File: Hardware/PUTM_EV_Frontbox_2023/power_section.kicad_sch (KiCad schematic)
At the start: 41 parts, among them U19 TLV743P, U20 LM4040DBZ-5, U4 TLV743P, U5 TLV743P, U6 BD50FC0FP, U7 LM62440-Q1

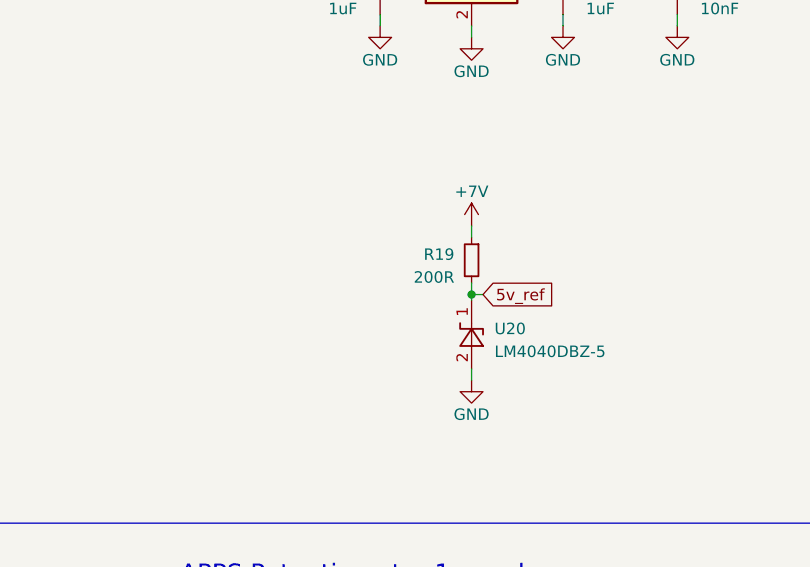
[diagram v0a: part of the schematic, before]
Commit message: Redid component placement
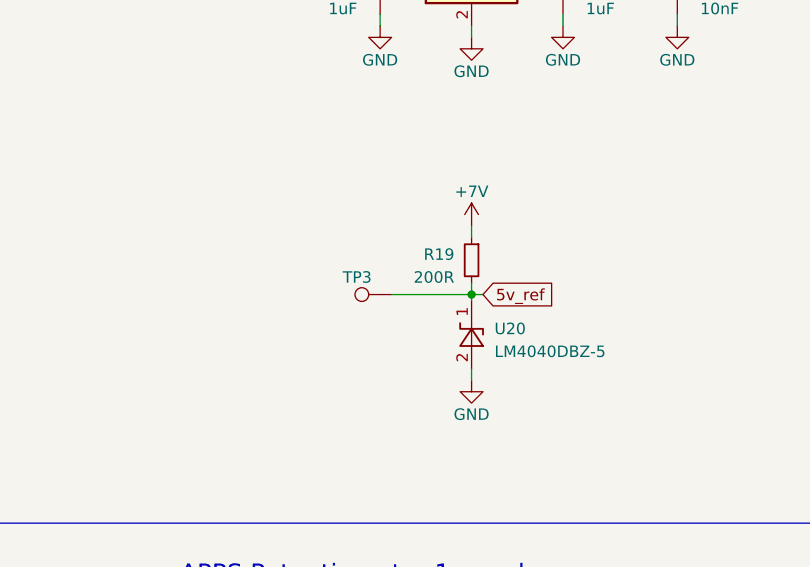
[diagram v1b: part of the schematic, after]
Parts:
- added TP3: TestPoint, TestPoint:TestPoint_Pad_1.0x1.0mm, symbol Connector:TestPoint
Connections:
- net 5v_ref: now also TP3.1
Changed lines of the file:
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@@
+    (stroke (width 0) (type default))
+  )
+  (wire (pts (xy 222.885 66.675) (xy 231.775 66.675))
     (stroke (width 0) (type default))
   )
@@
     )
   )
+  (symbol (lib_id "Connector:TestPoint") (at 222.885 66.675 90) (unit 1)
+    (in_bom yes) (on_board yes) (dnp no)
+    (property "Reference" "TP3" (at 219.075 64.77 90)
+      (effects (font (size 1.27 1.27)))
+    )
+    (property "Value" "TestPoint" (at 219.583 64.77 90)
+      (effects (font (size 1.27 1.27)) hide)
+    )
+    (property "Footprint" "TestPoint:TestPoint_Pad_1.0x1.0mm" (at 222.885 61.595 0)
+      (effects (font (size 1.27 1.27)) hide)
+    )
+    (property "Datasheet" "~" (at 222.885 61.595 0)
+      (effects (font (size 1.27 1.27)) hide)
+    )
+    (pin "1")
+    (instances
+      (project "PUTM_EV_Frontbox_2023"
+        (path "/b652b05a-4e3d-4ad1-b032-18886abe7d45/fd3e8671-032e-4b6a-9a43-a9c36a92201e"
+          (reference "TP3") (unit 1)
+        )
+      )
+    )
+  )
   (symbol (lib_id "Device:R_Small") (at 231.775 62.865 0) (mirror y) (unit 1)
     (in_bom yes) (on_board yes) (dnp no)
@@
       (effects (font (size 1.27 1.27)) hide)
     )
+    (pin "1")
+    (pin "10")
+    (pin "11")
+    (pin "12")
+    (pin "13")
+    (pin "14")
+    (pin "2")
     (pin "3")
-    (pin "1")
-    (pin "14")
+    (pin "4")
+    (pin "5")
+    (pin "6")
     (pin "7")
-    (pin "4")
-    (pin "6")
+    (pin "8")
     (pin "9")
-    (pin "11")
-    (pin "5")
-    (pin "13")
-    (pin "10")
-    (pin "2")
-    (pin "8")
-    (pin "12")
-    (instances
-      (project "PUTM_EV_Frontbox_2023"
+    (instances
+      (project "PUTM_EV_Frontbox_2023"

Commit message: PCB taken apart
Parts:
- removed C39: 10uF, Capacitor_SMD:CP_Elec_4x5.7, symbol Device:C_Polarized_Small
- removed R75: 220R, Resistor_SMD:R_0402_1005Metric, symbol Device:R_Small
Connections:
- net APPS_supply_1_3.3V: now also C14.1, U4.5 (OUT)
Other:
- moved on the sheet: C41, C43, C44, C45, C46, C47, D6, F4, L1, R87, R88, R89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

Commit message: Started PCB layout
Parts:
- removed F1: 1A, Fuse:Fuse_1812_4532Metric_Pad1.30x3.40mm_HandSolder, symbol Device:Polyfuse_Small
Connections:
- net +7.5V: now also C15.1, U6.1 (VCC)
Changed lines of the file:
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@@
     (stroke (width 0) (type default))
   )
-  (wire (pts (xy 206.375 29.21) (xy 202.565 29.21))
+  (wire (pts (xy 202.565 29.21) (xy 221.615 29.21))
     (stroke (width 0) (type default))
   )
@@
   )
   (wire (pts (xy 33.655 165.1) (xy 33.655 165.735))
-    (stroke (width 0) (type default))
-  )
-  (wire (pts (xy 211.455 29.21) (xy 221.615 29.21))
     (stroke (width 0) (type default))
   )
@@
     (effects (font (size 1.27 1.27)) (justify left))
   )
-  (symbol (lib_id "Device:Polyfuse_Small") (at 208.915 29.21 90) (unit 1)
-    (in_bom yes) (on_board yes) (dnp no) (fields_autoplaced)
-    (property "Reference" "F1" (at 208.915 24.13 90)
-      (effects (font (size 1.27 1.27)))
-    )
-    (property "Value" "1A" (at 208.915 26.67 90)
-      (effects (font (size 1.27 1.27)))
-    )
-    (property "Footprint" "Fuse:Fuse_1812_4532Metric_Pad1.30x3.40mm_HandSolder" (at 213.995 27.94 0)
-      (effects (font (size 1.27 1.27)) (justify left) hide)
-    )
-    (property "Datasheet" "https://www.mouser.pl/ProductDetail/Bussmann-Eaton/PTS18128V110?qs=QmibqUXyDhRaoNdJZeFheA%3D%3D" (at 208.915 29.21 0)
-      (effects (font (size 1.27 1.27)) hide)
-    )
-    (pin "1")
-    (pin "2")
-    (instances
-      (project "PUTM_EV_Frontbox_2023"
-        (path "/b652b05a-4e3d-4ad1-b032-18886abe7d45/fd3e8671-032e-4b6a-9a43-a9c36a92201e"
-          (reference "F1") (unit 1)
-        )
-      )
-    )
-  )
   (symbol (lib_id "power:GND") (at 241.935 36.83 0) (unit 1)

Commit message: Production files
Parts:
- removed C41, C44: 220nF, Capacitor_SMD:C_0402_1005Metric_Pad0.74x0.62mm_HandSolder, symbol Device:C_Small
- removed C43: 1uF, Capacitor_SMD:C_0402_1005Metric_Pad0.74x0.62mm_HandSolder, symbol Device:C_Small
- removed C45: 4u7F, Capacitor_SMD:CP_Elec_4x5.7, symbol Device:C_Small
- removed C46: 100nF, Capacitor_SMD:C_0402_1005Metric_Pad0.74x0.62mm_HandSolder, symbol Device:C_Small
- removed C47: 10uF, Capacitor_SMD:CP_Elec_4x5.7, symbol Device:C_Polarized_Small
- removed D6: SD24_SOD323, Diode_SMD:D_SOD-323_HandSoldering, symbol Diode:SD24_SOD323
- removed F4: 1.5A, Fuse:Fuse_1812_4532Metric_Pad1.30x3.40mm_HandSolder, symbol Device:Fuse_Small
- removed L1: 2u2H, Inductor_SMD:L_Abracon_ASPI-4030S, symbol Device:L_Small
- removed R19: 200R, Resistor_SMD:R_0402_1005Metric, symbol Device:R_Small
- removed R87: 100k, Resistor_SMD:R_0402_1005Metric, symbol Device:R_Small
- removed R88: 16k7, Resistor_SMD:R_0402_1005Metric, symbol Device:R_Small
- removed R89: 0R, Resistor_SMD:R_0402_1005Metric, symbol Device:R_Small
- removed TP3: TestPoint, TestPoint:TestPoint_Pad_1.0x1.0mm, symbol Connector:TestPoint
- removed U20: LM4040DBZ-5, Package_TO_SOT_SMD:SOT-23, symbol Reference_Voltage:LM4040DBZ-5
- removed U6: BD50FC0FP, Package_TO_SOT_SMD:TO-252-2, symbol Regulator_Linear:BD50FC0FP
- removed U7: LM62440-Q1, Frontbox:IC_LM61460AANRJRR, symbol LMR51420:LM62440
- added C10, C11: 2u2, Capacitor_SMD:C_0805_2012Metric, symbol Device:C_Small
- added C12, C13: 4u7, Capacitor_SMD:C_0805_2012Metric, symbol Device:C_Small
- added C14: 220n, Capacitor_SMD:C_0805_2012Metric, symbol Device:C_Small
- added C18: 22p, Capacitor_SMD:C_0603_1608Metric, symbol Device:C_Small
- added C19, C20: 22u, Capacitor_SMD:C_0603_1608Metric, symbol Device:C_Small
- added F1: 1.5A, Fuse:Fuse_1812_4532Metric, symbol Device:Polyfuse_Small
- added L2, L3: 1u5, Inductor_SMD:L_Abracon_ASPI-4030S, symbol Device:L
- added R3: 100k, Resistor_SMD:R_0603_1608Metric, symbol Device:R_Small
- added R4: 24k9, Resistor_SMD:R_0603_1608Metric, symbol Device:R_Small
- added R5: 1k, Resistor_SMD:R_0603_1608Metric, symbol Device:R_Small
- added TP2, TP4, TP5: TestPoint_Small, TestPoint:TestPoint_Pad_D1.0mm, symbol Connector:TestPoint_Small
- added U3: LM62440-Q1, footprints:IC_LM61460AANRJRR, symbol LM62440:LM62440
- C15: value 1uF -> 1u; footprint Capacitor_SMD:C_0402_1005Metric_Pad0.74x0.62mm_HandSolder -> Capacitor_SMD:C_0603_1608Metric
- C16: value 1uF -> 220n; footprint Capacitor_SMD:C_0402_1005Metric_Pad0.74x0.62mm_HandSolder -> Capacitor_SMD:C_0805_2012Metric; Rated Voltage (none) -> 35V
- C17: value 10nF -> 100n; footprint Capacitor_SMD:C_0402_1005Metric_Pad0.74x0.62mm_HandSolder -> Capacitor_SMD:C_0603_1608Metric
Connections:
- net +24V: now also F1.1
- net +5V: now also C19.1, C20.1, L3.2, R3.1, R5.1, TP5.1, U3.1 (BIAS); no longer C16.1, C17.1
- net GND: now also C10.2, C11.2, C12.2, C13.2, C14.2, C19.2, C20.2, R4.2, U3.11 (PGND2), U3.3 (AGND), U3.6 (MODE/SYNC), U3.9 (PGND1); no longer C17.2
- net +7.5V: no longer names the net of C15.1
- net +7.5V: now also U3.2 (VCC)
- new net: C18.1, R5.2
- new net: C17.2, U3.13 (RBOOT), U3.14 (CBOOT)
- new net +24V_FUSED: C10.1, C11.1, F1.2, L2.1
- new net FB: C18.2, R3.2, R4.1, TP4.1, U3.4 (FB)
- new net SW: C17.1, L3.1, U3.10 (SW)
- new net VIN: C12.1, C13.1, C14.1, C16.1, L2.2, TP2.1, U3.12 (VIN2), U3.7 (EN), U3.8 (VIN1)
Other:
- note added: "V_{out} = 5 V"
- note removed: "Supplies 5V ICs, Suspension potentiometers"

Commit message: New firmware
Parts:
- renumbered C10 to C1, C12 to C40, C13 to C41, C14 to C43, C15 to C44, C16 to C45, C17 to C46, C18 to C47, C11 to C5, C19 to C59, C20 to C60, L2 to L1, L3 to L2, R3 to R85, R4 to R86, R5 to R87, U3 to U7
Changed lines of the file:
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@@
   (symbol (lib_id "power:PWR_FLAG") (at 163.195 64.77 270) (unit 1)
     (in_bom yes) (on_board yes) (dnp no)
-    (property "Reference" "#FLG06" (at 165.1 64.77 0)
+    (property "Reference" "#FLG010" (at 165.1 64.77 0)
       (effects (font (size 1.27 1.27)) hide)
     )
@@
   (symbol (lib_id "Device:C_Small") (at 90.805 78.74 0) (unit 1)
     (in_bom yes) (on_board yes) (dnp no)
-    (property "Reference" "C15" (at 88.265 77.47 0)
+    (property "Reference" "C44" (at 88.265 77.47 0)
       (effects (font (size 1.27 1.27)) (justify right))
     )
@@
   (symbol (lib_id "power:GND") (at 121.285 50.8 0) (unit 1)
     (in_bom yes) (on_board yes) (dnp no)
-    (property "Reference" "#PWR031" (at 121.285 57.15 0)
+    (property "Reference" "#PWR0153" (at 121.285 57.15 0)
       (effects (font (size 1.27 1.27)) hide)
     )
@@
   (symbol (lib_id "Device:C_Small") (at 33.655 43.18 0) (mirror y) (unit 1)
     (in_bom yes) (on_board yes) (dnp no)
-    (property "Reference" "C10" (at 36.195 40.64 0)
+    (property "Reference" "C1" (at 36.195 40.64 0)
       (effects (font (size 1.27 1.27)) (justify right))
     )
@@
   (symbol (lib_id "Connector:TestPoint_Small") (at 161.925 64.77 0) (unit 1)
     (in_bom yes) (on_board yes) (dnp no)
-    (property "Reference" "TP?" (at 160.655 63.5 0)
+    (property "Reference" "TP5" (at 160.655 63.5 0)
       (effects (font (size 1 1)) (justify right))
     )
@@
   (symbol (lib_id "Device:R_Small") (at 141.605 68.58 0) (unit 1)
     (in_bom yes) (on_board yes) (dnp no)
-    (property "Reference" "R5" (at 144.145 67.31 0)
+    (property "Reference" "R87" (at 144.145 67.31 0)
       (effects (font (size 1.27 1.27)) (justify left))
     )
@@
   (symbol (lib_id "Device:L") (at 55.245 38.1 90) (unit 1)
     (in_bom yes) (on_board yes) (dnp no)
-    (property "Reference" "L2" (at 55.245 35.56 90)
+    (property "Reference" "L1" (at 55.245 35.56 90)
       (effects (font (size 1.27 1.27)))
     )
@@
   (symbol (lib_id "Device:L") (at 126.365 64.77 90) (unit 1)
     (in_bom yes) (on_board yes) (dnp no)
-    (property "Reference" "L3" (at 125.095 62.865 90)
+    (property "Reference" "L2" (at 125.095 62.865 90)
       (effects (font (size 1.27 1.27)))
     )
@@
   (symbol (lib_id "power:GND") (at 90.805 64.77 0) (unit 1)
     (in_bom yes) (on_board yes) (dnp no)
-    (property "Reference" "#PWR028" (at 90.805 71.12 0)
+    (property "Reference" "#PWR0150" (at 90.805 71.12 0)
       (effects (font (size 1.27 1.27)) hide)
     )
@@
   (symbol (lib_id "Device:C_Small") (at 62.865 43.18 0) (mirror y) (unit 1)
     (in_bom yes) (on_board yes) (dnp no)
-    (property "Reference" "C12" (at 65.405 40.64 0)
+    (property "Reference" "C40" (at 65.405 40.64 0)
       (effects (font (size 1.27 1.27)) (justify right))
     )
@@
   (symbol (lib_id "Device:C_Small") (at 151.765 68.58 0) (mirror y) (unit 1)
     (in_bom yes) (on_board yes) (dnp no)
-    (property "Reference" "C19" (at 154.305 67.31 0)
+    (property "Reference" "C59" (at 154.305 67.31 0)
       (effects (font (size 1.27 1.27)) (justify right))
     )
@@
   (symbol (lib_id "power:+5V") (at 161.925 63.5 0) (unit 1)
     (in_bom yes) (on_board yes) (dnp no)
-    (property "Reference" "#PWR034" (at 161.925 67.31 0)
+    (property "Reference" "#PWR0156" (at 161.925 67.31 0)
       (effects (font (size 1.27 1.27)) hide)
     )
@@
   (symbol (lib_id "Device:C_Small") (at 45.085 43.18 0) (mirror y) (unit 1)
     (in_bom yes) (on_board yes) (dnp no)
-    (property "Reference" "C11" (at 47.625 40.64 0)
+    (property "Reference" "C5" (at 47.625 40.64 0)
       (effects (font (size 1.27 1.27)) (justify right))
     )
@@
   (symbol (lib_id "Device:C_Small") (at 161.925 68.58 0) (mirror y) (unit 1)
     (in_bom yes) (on_board yes) (dnp no)
-    (property "Reference" "C20" (at 164.465 67.31 0)
+    (property "Reference" "C60" (at 164.465 67.31 0)
       (effects (font (size 1.27 1.27)) (justify right))
     )
@@
   (symbol (lib_id "Connector:TestPoint_Small") (at 131.445 77.47 0) (unit 1)
     (in_bom yes) (on_board yes) (dnp no)
-    (property "Reference" "TP?" (at 130.175 76.2 0)
+    (property "Reference" "TP4" (at 130.175 76.2 0)
       (effects (font (size 1 1)) (justify right))
     )
@@
   (symbol (lib_id "Device:C_Small") (at 121.285 46.99 0) (mirror y) (unit 1)
     (in_bom yes) (on_board yes) (dnp no)
-    (property "Reference" "C16" (at 123.825 44.45 0)
+    (property "Reference" "C45" (at 123.825 44.45 0)
       (effects (font (size 1.27 1.27)) (justify right))
     )
@@
   (symbol (lib_id "Device:C_Small") (at 73.025 43.18 0) (mirror y) (unit 1)
     (in_bom yes) (on_board yes) (dnp no)
-    (property "Reference" "C13" (at 75.565 40.64 0)
+    (property "Reference" "C41" (at 75.565 40.64 0)
       (effects (font (size 1.27 1.27)) (justify right))
     )
@@
   (symbol (lib_id "Connector:TestPoint_Small") (at 81.915 38.1 0) (unit 1)
     (in_bom yes) (on_board yes) (dnp no)
-    (property "Reference" "TP?" (at 80.645 36.83 0)
+    (property "Reference" "TP2" (at 80.645 36.83 0)
       (effects (font (size 1 1)) (justify right))
     )
@@
   (symbol (lib_id "Device:R_Small") (at 131.445 73.66 0) (unit 1)
     (in_bom yes) (on_board yes) (dnp no)
-    (property "Reference" "R3" (at 132.715 69.85 0)
+    (property "Reference" "R85" (at 132.715 69.85 0)
       (effects (font (size 1.27 1.27)) (justify left))
     )
@@
   (symbol (lib_id "power:+24V") (at 20.955 36.83 0) (unit 1)
     (in_bom yes) (on_board yes) (dnp no)
-    (property "Reference" "#PWR021" (at 20.955 40.64 0)
+    (property "Reference" "#PWR044" (at 20.955 40.64 0)
       (effects (font (size 1.27 1.27)) hide)
     )
@@
   (symbol (lib_id "power:PWR_FLAG") (at 81.915 36.83 0) (unit 1)
     (in_bom yes) (on_board yes) (dnp no) (fields_autoplaced)
-    (property "Reference" "#FLG05" (at 81.915 34.925 0)
+    (property "Reference" "#FLG09" (at 81.915 34.925 0)
       (effects (font (size 1.27 1.27)) hide)
     )
@@
   (symbol (lib_id "Device:C_Small") (at 141.605 73.66 0) (mirror y) (unit 1)
     (in_bom yes) (on_board yes) (dnp no)
-    (property "Reference" "C18" (at 144.145 72.39 0)
+    (property "Reference" "C47" (at 144.145 72.39 0)
       (effects (font (size 1.27 1.27)) (justify right))
     )
@@
   (symbol (lib_id "power:PWR_FLAG") (at 19.685 38.1 90) (unit 1)
     (in_bom yes) (on_board yes) (dnp no) (fields_autoplaced)
-    (property "Reference" "#FLG03" (at 17.78 38.1 0)
+    (property "Reference" "#FLG02" (at 17.78 38.1 0)
       (effects (font (size 1.27 1.27)) hide)
     )
@@
   (symbol (lib_id "Device:R_Small") (at 131.445 81.28 0) (unit 1)
     (in_bom yes) (on_board yes) (dnp no)
-    (property "Reference" "R4" (at 132.715 80.01 0)
+    (property "Reference" "R86" (at 132.715 80.01 0)
       (effects (font (size 1.27 1.27)) (justify left))
     )
@@
   (symbol (lib_id "LM62440:LM62440") (at 106.045 60.96 0) (unit 1)
     (in_bom yes) (on_board yes) (dnp no)
-    (property "Reference" "U3" (at 95.885 40.64 0)
+    (property "Reference" "U7" (at 95.885 40.64 0)
       (effects (font (size 1.27 1.27)) (justify left))
     )
@@
   (symbol (lib_id "Device:C_Small") (at 121.285 67.31 0) (mirror y) (unit 1)
     (in_bom yes) (on_board yes) (dnp no)
-    (property "Reference" "C17" (at 123.825 67.31 0)
+    (property "Reference" "C46" (at 123.825 67.31 0)
       (effects (font (size 1.27 1.27)) (justify right))
     )
@@
   (symbol (lib_id "Device:C_Small") (at 90.805 46.99 0) (unit 1)
     (in_bom yes) (on_board yes) (dnp no)
-    (property "Reference" "C14" (at 88.265 44.45 0)
-      (effects (font (size 1.27 1.27)) (justify right))
-    )
+    (property "Reference" "C43" (at 88.265 44.45 0)
+      (effects (font (size 1.27 1.27)) (justify right))
+    )
